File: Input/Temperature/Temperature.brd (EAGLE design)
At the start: 20 x 13 mm, 10 parts, among them U5 TMP006AIYZFR

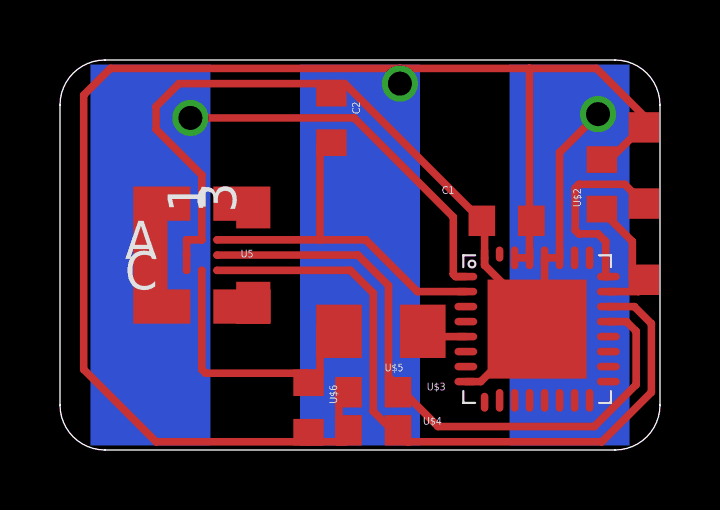
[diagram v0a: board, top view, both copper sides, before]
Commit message: Update Pinheader
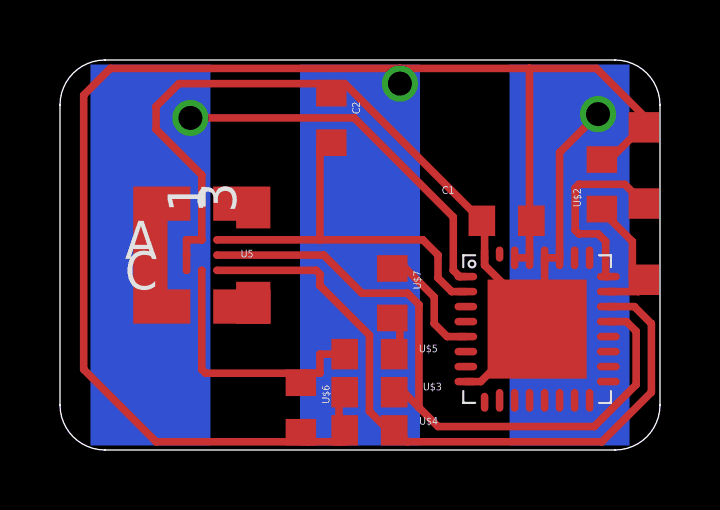
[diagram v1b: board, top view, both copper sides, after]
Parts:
- added U$7: 0k, thar:603
- U$5: device thar:1206 -> thar:603
- moved U$5 0.85 mm to (12.1, 4.45)
- moved U$6 0.25 mm to (9.78, 2.67)
- moved U$3 0.13 mm to (12.1, 3.17)
- moved U$4 0.13 mm to (12.1, 1.91)
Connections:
- new net N$11: U$5.1, U$7.2
- net N$2: now also U$7.1; no longer U$5.1
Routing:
- net N$2: track 1.48 -> 3.91 mm
- net N$11: track 0.00 -> 1.69 mm
- net N$6: track 22.0 -> 23.2 mm
- net N$5: track 23.8 -> 23.2 mm
- net N$14: track 10.1 -> 9.47 mm
